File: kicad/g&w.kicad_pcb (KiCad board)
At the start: 2 copper layers, 181 parts, among them IC1 audio, IC2 MX25U8035F, IC3 vreg, IC4 pmic, IC5 BQ24072RGT_, J1 speaker, J2 SWD PORT, J3 DISPLAY1, J4 DISPLAY2, J5 Battery, J6 USB-C, Q1 PMBT3904, Q2 PMBT3904, Q3 PMBT3904, Q4 SSM6J412TU, Y1 H01717

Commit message: kicad board outline
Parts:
- added H51: MountingHole_Pad, gnw:MountingHole_2.0mm, F.Cu at (2.35, 2.50)
- added H52: MountingHole_Pad, gnw:MountingHole_2.0mm, F.Cu at (3.60, 20.5)
- added H53: MountingHole, gnw:MountingSlot_NC_1.3x2.2mm, F.Cu at (-2.00, 25.0)
- added H54: MountingHole_Pad, gnw:MountingHole_2.0mm, F.Cu at (25.5, 5.00)
- added H55: MountingHole_Pad, gnw:MountingHole_2.0mm, F.Cu at (21.8, 19.2)
- added H56: MountingHole, gnw:MountingHole_NC_1.5mm, F.Cu at (120.1, 31.8)
- added H57: MountingHole_Pad, gnw:MountingHole_2.0mm, F.Cu at (111.9, 4.44)
- added H58: MountingHole_Pad, gnw:MountingHole_2.0mm, F.Cu at (80.4, 29.8)
- added H59: MountingHole_Pad, gnw:MountingHole_2.0mm, F.Cu at (111.6, 11.8)
- added H60: MountingHole_Pad, gnw:MountingHole_2.0mm, F.Cu at (76.9, 49.9)
- moved JP81 145.1 mm to (74.3, -3.69)
- moved R30 145.1 mm to (74.0, -1.79)
- moved TP70 145.1 mm to (71.4, -2.04)
- moved B7 144.5 mm to (75.1, 44.9)
- moved B8 144.5 mm to (75.8, 54.8)
- moved JP97 144.5 mm to (71.2, 44.5)
- moved JP98 144.5 mm to (72.1, 54.5)
- moved JP99 144.5 mm to (72.5, 64.4)
- moved TP80 144.5 mm to (72.8, 66.5)
- moved B9 144.5 mm to (76.4, 64.9)
- moved TP78 144.5 mm to (71.5, 46.1)
- moved TP79 144.5 mm to (72.5, 55.8)
- moved J5 144.3 mm to (69.0, -4.20), turned to 270 degrees
- moved C27 142.9 mm to (70.1, -11.6)
- moved C30 142.9 mm to (75.6, -8.07)
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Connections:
- net BAT-MESS-p32-PC4 renamed BAT-MEAS-p32-PC4
- IC1 pad A2: Net-(IC1-PadA2) -> GND
- IC1 pad C3: Net-(IC1-PadA2) -> GND
- JP78 pad 1: Net-(IC1-PadA2) -> GND
- JP79 pad 1: Net-(IC1-PadA2) -> GND
- JP86 pad 1: Net-(IC1-PadA2) -> GND
- JP87 pad 1: Net-(IC1-PadA2) -> GND
- R1 pad 1: Net-(IC1-PadA2) -> GND
- R2 pad 2: Net-(IC1-PadA2) -> GND
- R3 pad 1: Net-(IC1-PadA2) -> GND
- R4 pad 2: Net-(IC1-PadA2) -> GND
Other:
- board outline added: 108.7 x 55 mm
- net class Default: clearance 0.2 -> 0.254; trace_width 0.25 -> 0.15; via_dia 0.8 -> 0.6; via_drill 0.4 -> 0.3
- rule trace_clearance: 0.2 -> 0.254
- rule trace_min: 0.2 -> 0.13
- rule via_min_size: 0.4 -> 0.5

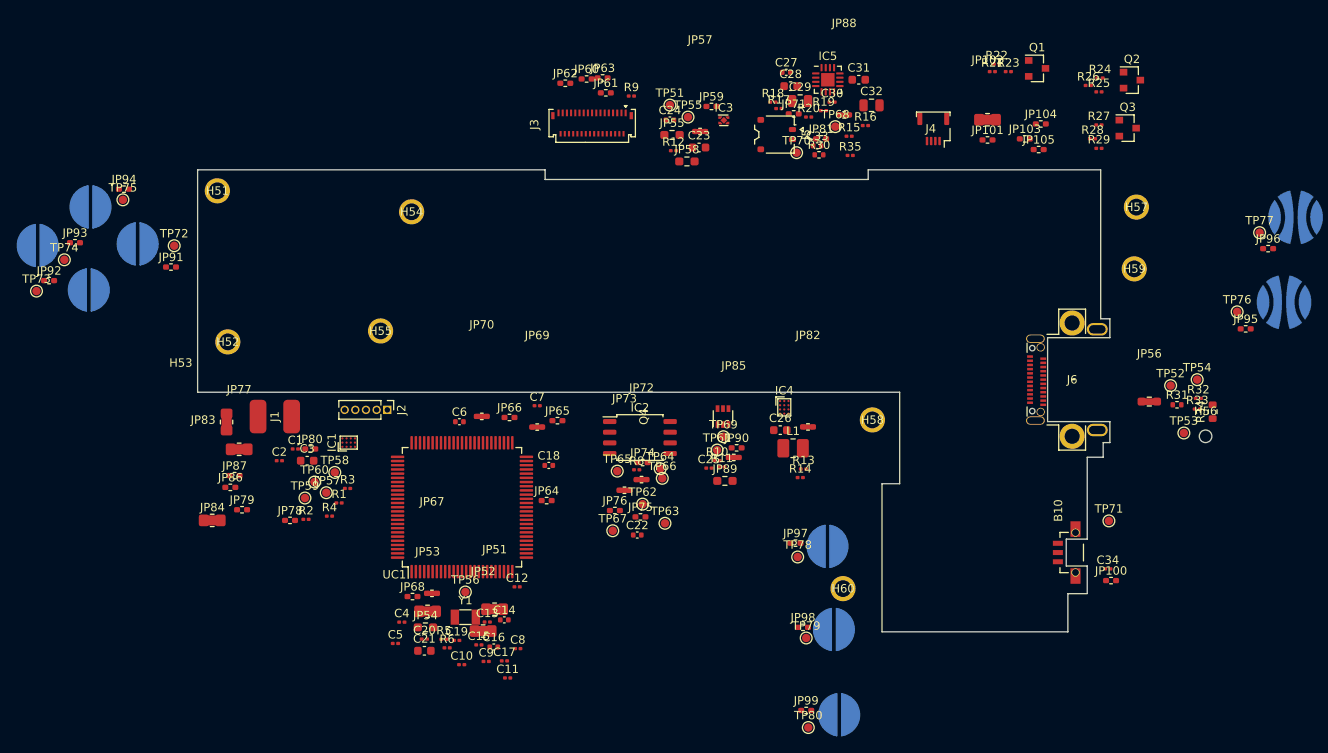
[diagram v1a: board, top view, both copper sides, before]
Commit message: tweak footprints, setup design rules for 4 layers at common proto board house and refine board outline
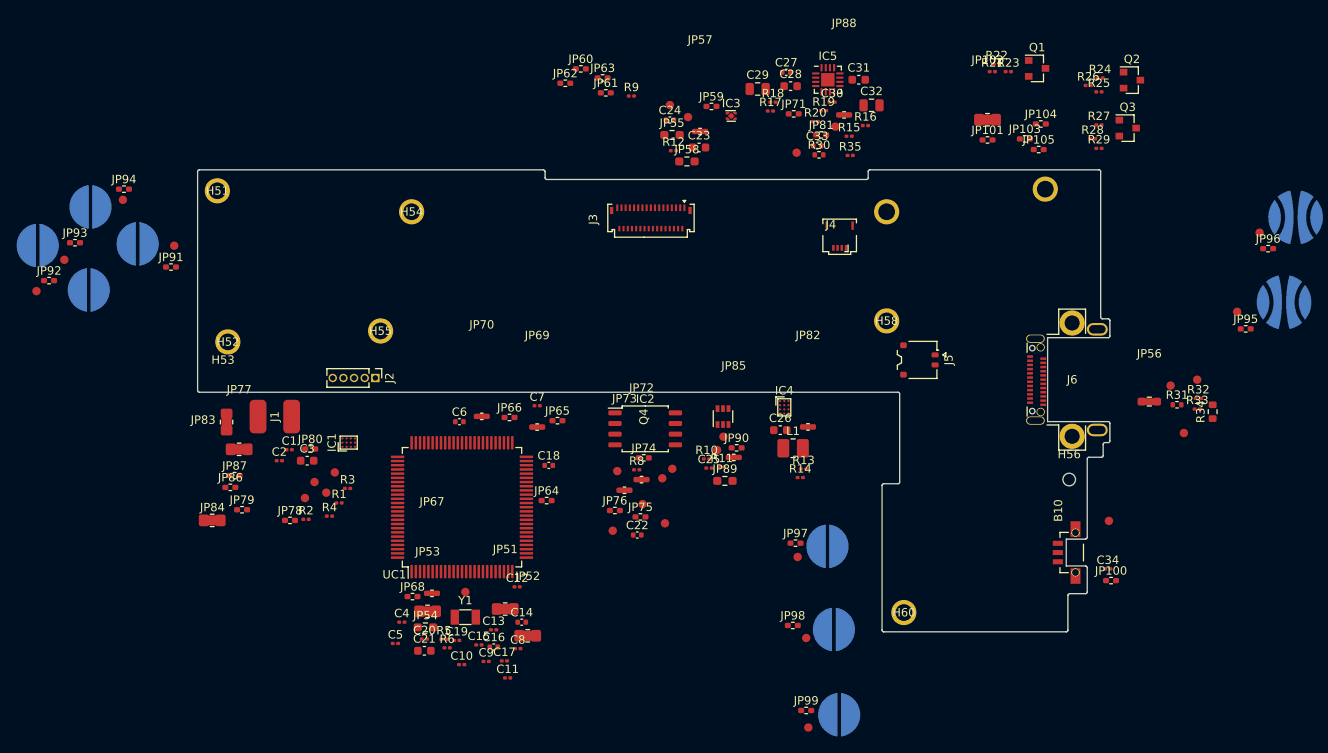
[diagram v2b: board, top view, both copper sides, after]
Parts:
- TP51, TP52, TP53, TP54, TP55, TP56, TP57, TP58, TP59, TP60, TP61, TP62, TP63, TP64, TP65, TP66, TP67, TP68, TP69, TP70, TP71, TP72, TP73, TP74, TP75, TP76, TP77, TP78, TP79, TP80: footprint TestPoint:TestPoint_Pad_D1.0mm -> gnw:gnw-TestPoint_Pad_D1.0mm
- moved J5 31.8 mm to (86.0, 22.6)
- moved H59 30.3 mm to (82.1, 5.00)
- moved H56 17.0 mm to (103.8, 36.9)
- moved J4 16.5 mm to (76.5, 8.00)
- moved J3 13.3 mm to (54.0, 5.80)
- moved H58 11.9 mm to (82.1, 18.0)
- moved H57 11.1 mm to (101.0, 2.30)
- moved H60 7.79 mm to (84.2, 52.8)
- moved JP52 5.34 mm to (39.3, 55.5)
- moved C29 5.26 mm to (66.7, -9.63)
- moved H53 5.04 mm to (3.02, 24.6)
- moved J2 4.06 mm to (21.2, 24.8)
- moved C14 2.09 mm to (38.6, 53.9)
- moved TP64 1.45 mm to (56.6, 35.6)
- moved JP60 1.39 mm to (45.7, -12.0)
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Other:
- board size 108.7 x 55 mm -> 108.7 x 55.1 mm
- copper layers 2 -> 4
- net class Default: clearance 0.254 -> 0.09
- rule trace_clearance: 0.254 -> 0.09

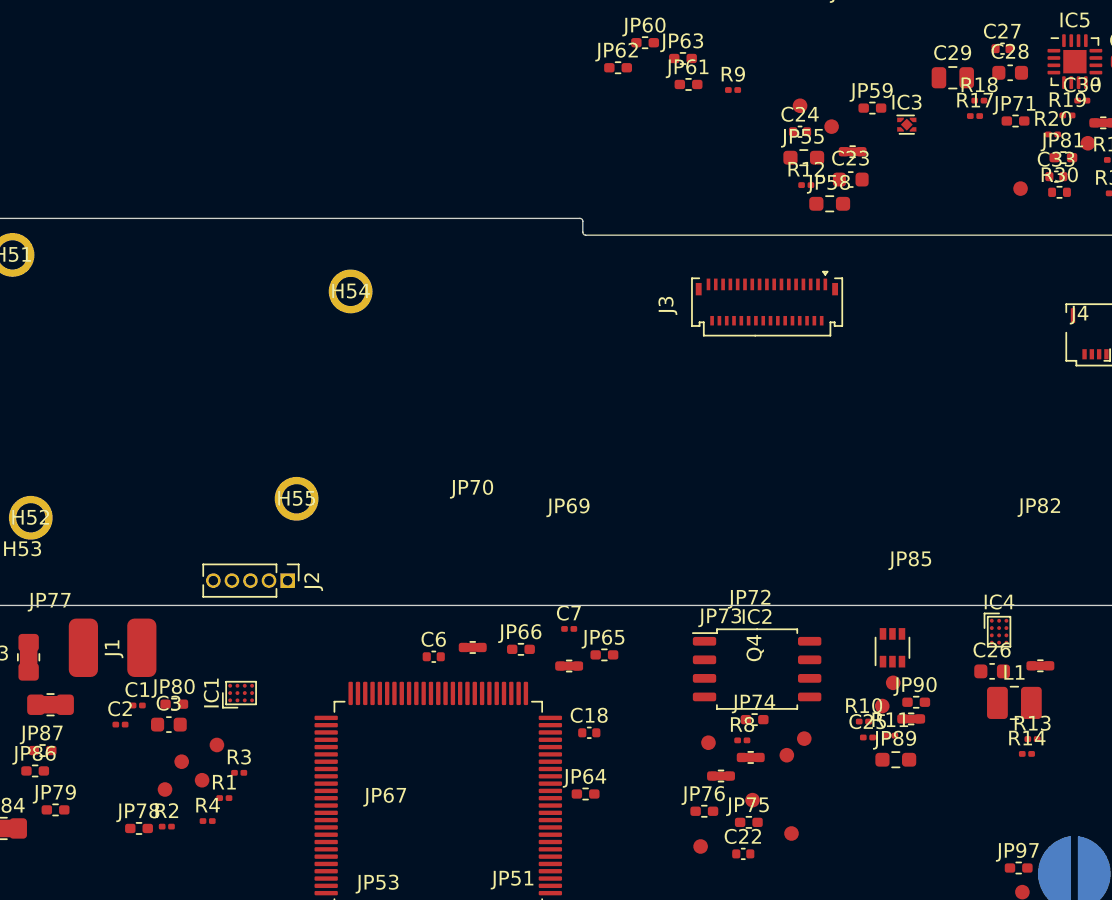
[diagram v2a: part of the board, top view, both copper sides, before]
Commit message: Updated Trace&Schematic with new parts numbers. Made new footprints for both BGA's and 3v3 reg. Still need to revise USB-C connector footprint.
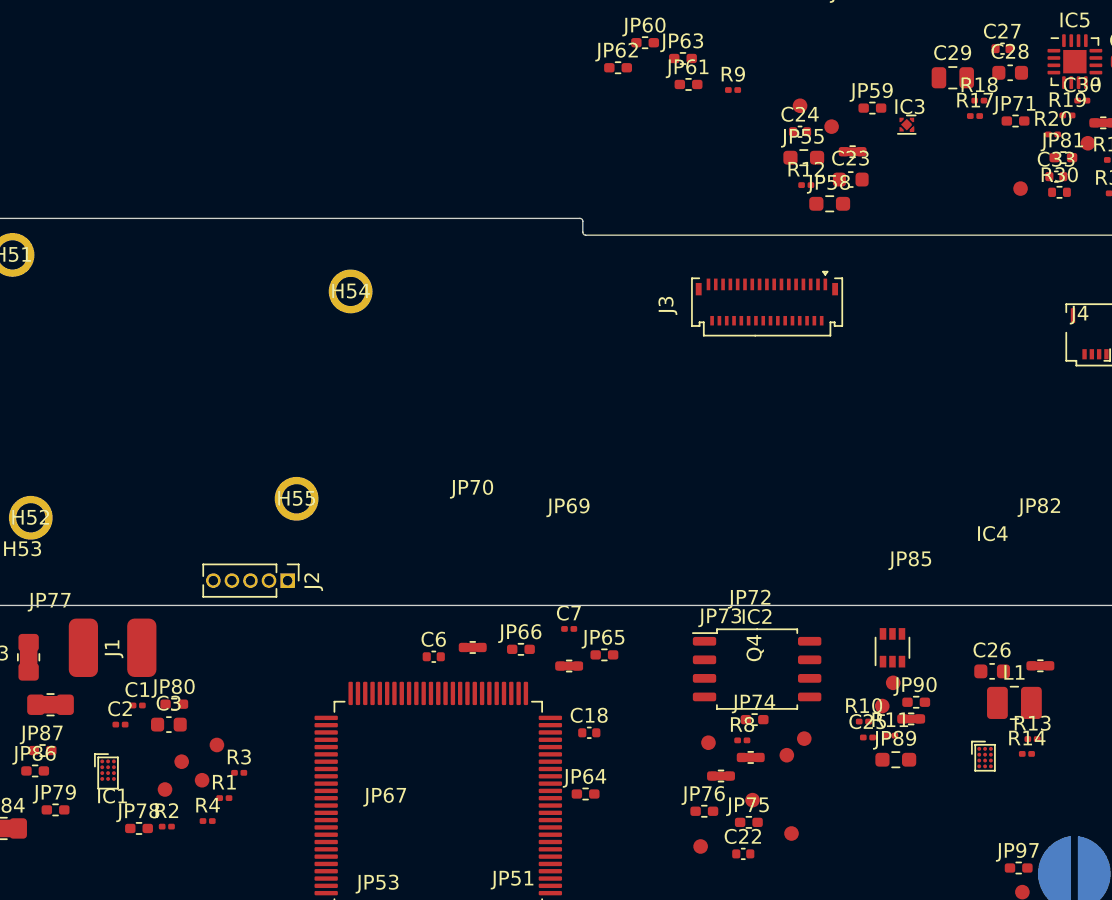
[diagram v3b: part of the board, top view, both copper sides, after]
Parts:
- IC1: value audio -> NAU8315-B31V; footprint Package_BGA:Texas_DSBGA-12_1.36x1.86mm_Layout3x4_P0.5mm -> gnw:WLCSP-12_1.18x1.95_Layout3x4_P0.4mm
- IC2: value MX25U8035F -> MX25U8035FM2
- IC3: value vreg -> LD39020DTPU33R; footprint Package_SON:Texas_X2SON-4_1x1mm_P0.65mm -> gnw:DFN-4-1EP_1x1_P0.65mm_EP0.56x0.56mm
- IC4: value pmic -> DA9230-61VZ2; footprint Package_BGA:Texas_DSBGA-12_1.36x1.86mm_Layout3x4_P0.5mm -> gnw:WLCSP-12_1.28x1.68_Layout3x4_P0.4mm
- IC5: value BQ24072RGT_ -> BQ24072RGT
- L1: value UNKNOWN -> 2R2M
- moved IC1 10.5 mm to (8.89, 37.8), turned to 0 degrees
- moved IC4 8.67 mm to (68.9, 36.9)
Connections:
- IC1 pad C2: Net-(IC1-PadC2) -> Net-(IC1-PadB2)
- IC1 pad D2: V3v7 -> Net-(IC1-PadB2)

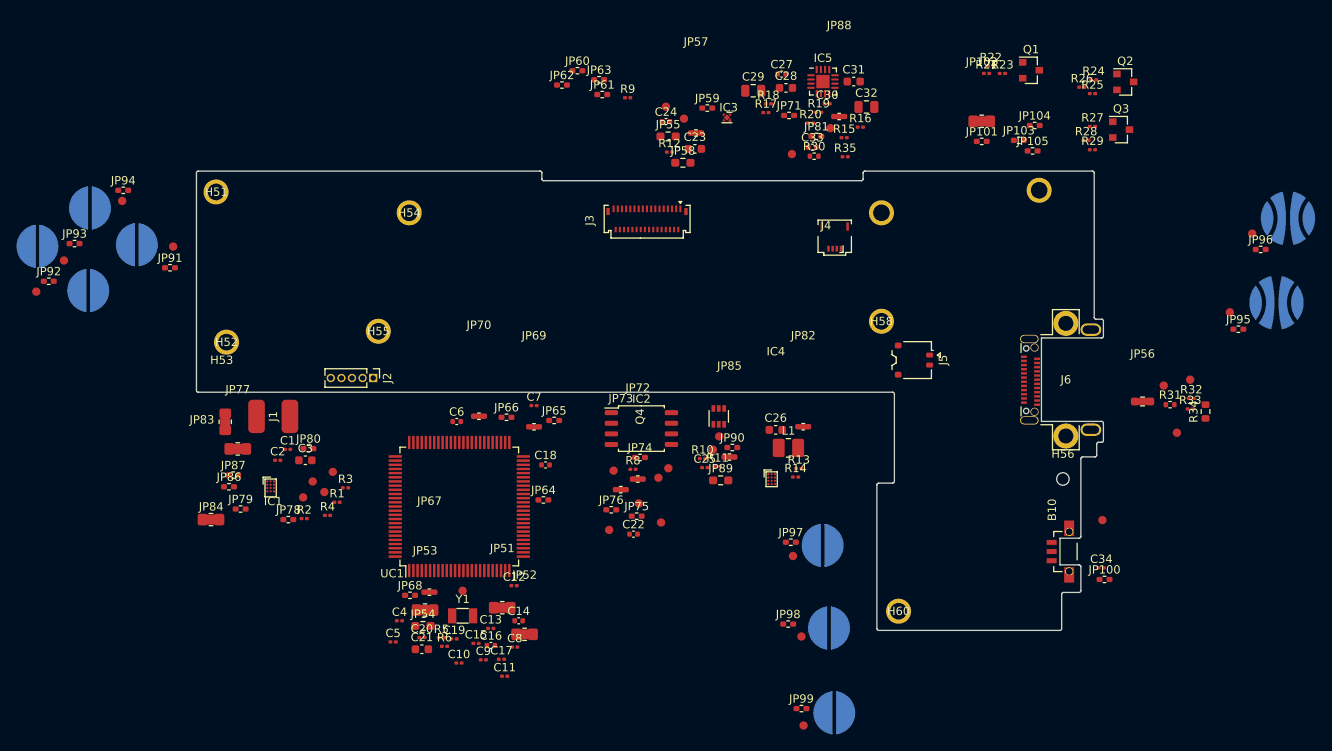
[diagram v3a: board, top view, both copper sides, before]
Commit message: USB-C footprint updated from datasheet drawing 1:1 with critical dimensions layer in PCBnew
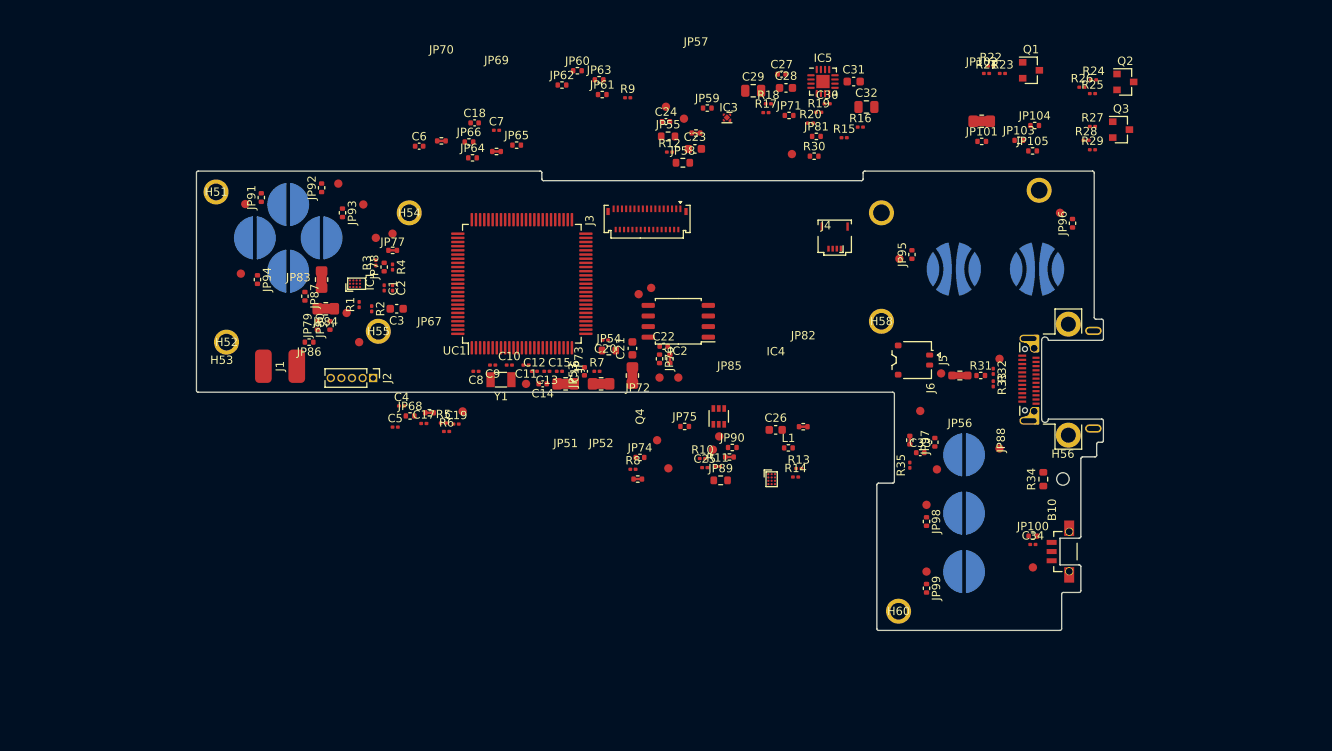
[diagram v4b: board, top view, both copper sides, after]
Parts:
- added R7: 100k, Resistor_SMD:R_0201_0603Metric, F.Cu at (48.0, 24.0)
- added TP81: TestPoint, gnw:gnw-TestPoint_Pad_D1.0mm, F.Cu at (39.5, 25.5)
- J6: footprint gnw:USB_C_Receptacle_NintendoG&W -> gnw:USB_C_Receptacle_JAE_DX07BN24JA2
- JP100, JP101, JP103, JP104, JP105, JP59, JP60, JP61, JP62, JP63, JP64, JP65, JP66, JP68, JP71, JP74, JP75, JP76, JP78, JP79, JP80, JP81, JP86, JP87, JP90, JP91, JP92, JP93, JP94, JP95, JP96, JP97, JP98, JP99: footprint Resistor_SMD:R_0402_1005Metric_Pad0.72x0.64mm_HandSolder -> Resistor_SMD:R_0402_1005Metric
- JP54, JP55, JP58, JP89: footprint Resistor_SMD:R_0603_1608Metric_Pad0.98x0.95mm_HandSolder -> Resistor_SMD:R_0603_1608Metric
- JP77: value jmp-0805 -> JMP-0402-CLOSED; footprint gnw:JMP-0805-CLOSED -> gnw:JMP-0402-CLOSED
- L1: footprint Inductor_SMD:L_1008_2520Metric_Pad1.43x2.20mm_HandSolder -> Resistor_SMD:R_0402_1005Metric
- moved C21 44.0 mm to (52.2, 21.2), turned to 90 degrees
- moved C20 41.9 mm to (49.0, 20.2), turned to 180 degrees
- moved C18 41.9 mm to (33.3, -5.78)
- moved JP64 41.9 mm to (33.1, -1.59)
- moved JP95 40.1 mm to (85.8, 10.0), turned to 90 degrees
- moved TP76 40.1 mm to (84.2, 10.5)
- moved JP54 39.8 mm to (49.4, 21.5)
- moved JP88 39.7 mm to (85.5, 32.2), turned to 270 degrees
- moved B5 38.9 mm to (90.8, 11.8)
- moved C33 38.8 mm to (86.8, 33.8)
- moved TP73 38.4 mm to (17.0, 1.50)
- moved R35 37.8 mm to (85.5, 35.2), turned to 90 degrees
- moved JP53 37.5 mm to (52.2, 24.5), turned to 90 degrees
- moved C11 37.4 mm to (39.5, 23.2), turned to 180 degrees
- moved TP74 36.5 mm to (20.0, 4.00)
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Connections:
- IC1 pad B2: Net-(IC1-PadB2) -> V3v7
- IC1 pad C2: Net-(IC1-PadB2) -> V3v7
- IC1 pad D2: Net-(IC1-PadB2) -> V3v7
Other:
- outline, holes or cut-outs redrawn
